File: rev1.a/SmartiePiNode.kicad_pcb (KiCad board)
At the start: 2 copper layers, 71.7 x 55 mm, 53 parts, among them CN1 USBMICROb, CN2 ST-LINK, CN3 SX1238_TRX_HEADER, SW1 SW_PUSH, U1 ISL91127IR, U2 STM32L052_LQFP48, X1 abm10, X2 ABS25-32.768KHZ-6-T

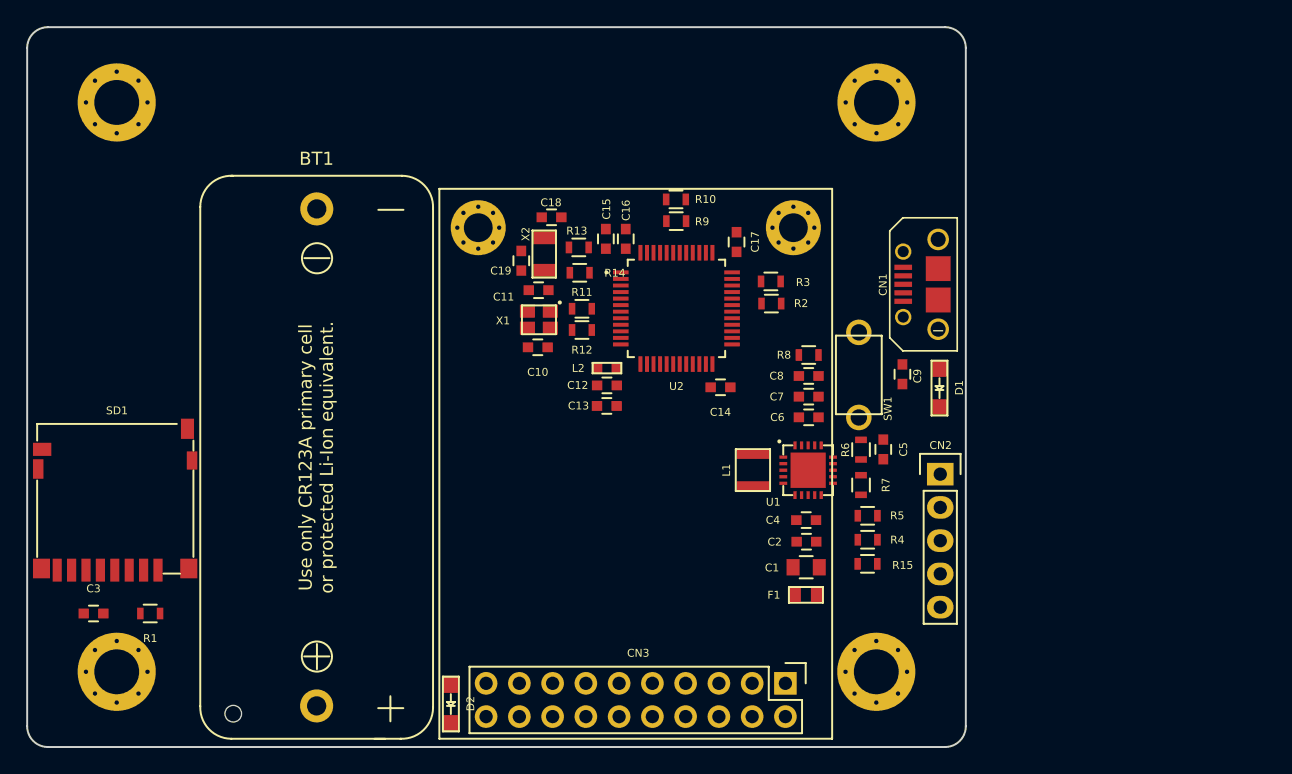
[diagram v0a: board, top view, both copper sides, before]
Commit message: footprint placement and tweaking continued...
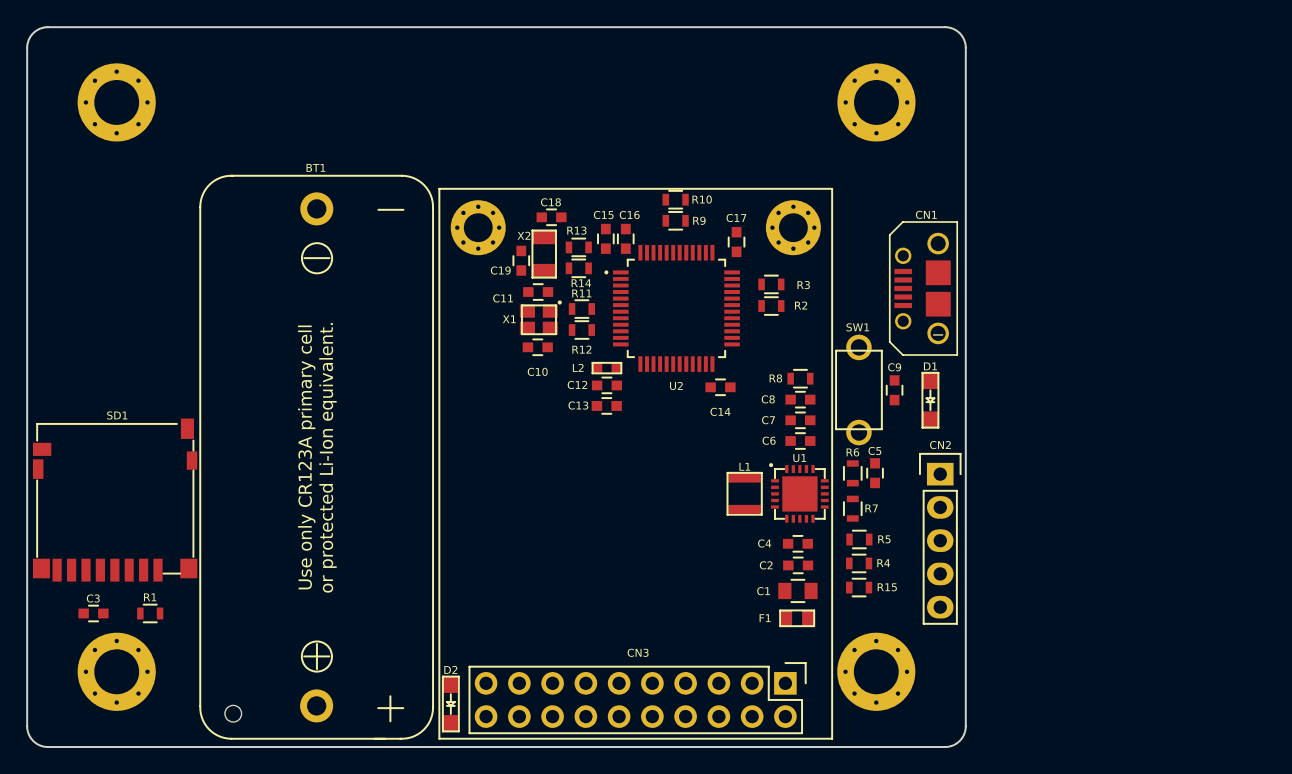
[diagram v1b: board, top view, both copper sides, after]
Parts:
- moved R4 1.92 mm to (162.6, 136.6), turned to 180 degrees
- moved R15 1.92 mm to (162.6, 138.5)
- moved U1 1.92 mm to (158.1, 131.3)
- moved C1 1.92 mm to (157.9, 138.7)
- moved C2 1.92 mm to (157.9, 136.8)
- moved C4 1.92 mm to (157.9, 135.1)
- moved C5 1.92 mm to (163.8, 129.7)
- moved C6 1.92 mm to (158.1, 127.3)
- moved C7 1.92 mm to (158.1, 125.7)
- moved L1 1.92 mm to (153.9, 131.3)
- moved R5 1.92 mm to (162.6, 134.8)
- moved R7 1.92 mm to (162.1, 132.5)
- moved R8 1.92 mm to (158.1, 122.5)
- moved C8 1.92 mm to (158.1, 124.1)
- moved R6 1.92 mm to (162.1, 129.8)
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
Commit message: usb and schematic changes/tweaks.
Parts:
- added CN4: VIN, Pin_Headers:Pin_Header_Straight_1x02, F.Cu at (168.8, 143.6)
- added R16: 100K, Resistors_SMD:R_0603, F.Cu at (163.6, 112.1)
- added R17: 1.5K, Resistors_SMD:R_0603, F.Cu at (163.6, 114.7)
- CN2: value ST-LINK -> SWD
- moved CN1 0.20 mm to (167.2, 115.8)

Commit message: added battery sensing circuit and a bit more work on usb.
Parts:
- added C20: DNP, Capacitors_SMD:C_0603, F.Cu at (181.1, 119.0)
- added R18: DNP, Resistors_SMD:R_0603, F.Cu at (181.1, 124.9)
- added R19: DNP, Resistors_SMD:R_0603, F.Cu at (184.7, 119.0)
- added R20: DNP, Resistors_SMD:R_0603, F.Cu at (188.3, 119.0)
- added R21: DNP, Resistors_SMD:R_0603, F.Cu at (191.9, 119.0)
- added R22: DNP, Resistors_SMD:R_0603, F.Cu at (184.7, 124.9)
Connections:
- R17 pad 1: /+3V3 -> /USB_RENUMn
- U2 pad 11: /+VBAT -> Net-(U2-Pad11)
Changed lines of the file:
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@@
 (kicad_pcb (version 20160815) (host pcbnew "(2017-01-24 revision 0b6147e)-makepkg")
   (general
-    (links 182)
-    (no_connects 134)
+    (links 189)
+    (no_connects 141)
     (area 98.984999 95.604999 170.825001 150.735001)
     (thickness 1.6)
@@
     (tracks 1)
     (zones 0)
-    (modules 56)
-    (nets 74)
+    (modules 62)
+    (nets 79)
   )
   (page A4)
@@
   (net 72 "Net-(R15-Pad1)")
   (net 73 "Net-(CN4-Pad1)")
+  (net 74 /VMEASURE)
+  (net 75 /USB_RENUMn)
+  (net 76 "Net-(R19-Pad2)")
+  (net 77 /VSENSE)
+  (net 78 "Net-(U2-Pad11)")
   (net_class Default "This is the default net class."
     (clearance 0.2)
@@
     (add_net /USB_DM)
     (add_net /USB_DP)
+    (add_net /USB_RENUMn)
+    (add_net /VMEASURE)
+    (add_net /VSENSE)
     (add_net GND)
     (add_net "Net-(C10-Pad2)")
@@
     (add_net "Net-(R14-Pad2)")
     (add_net "Net-(R15-Pad1)")
+    (add_net "Net-(R19-Pad2)")
     (add_net "Net-(R4-Pad1)")
     (add_net "Net-(SD1-Pad1)")
@@
     (add_net "Net-(U1-Pad16)")
     (add_net "Net-(U2-Pad10)")
+    (add_net "Net-(U2-Pad11)")
     (add_net "Net-(U2-Pad12)")
     (add_net "Net-(U2-Pad13)")
@@
       (net 69 "Net-(U2-Pad12)"))
     (pad 11 smd rect (at -4.249999 2.250001) (size 1.1938 0.3048) (layers F.Cu F.Paste F.Mask)
-      (net 2 /+VBAT))
+      (net 78 "Net-(U2-Pad11)"))
     (pad 10 smd rect (at -4.249999 1.749999) (size 1.1938 0.3048) (layers F.Cu F.Paste F.Mask)
       (net 70 "Net-(U2-Pad10)"))
@@
     (fp_line (start -0.5 -0.675) (end 0.5 -0.675) (layer F.SilkS) (width 0.15))
     (pad 1 smd rect (at -0.75 0 270) (size 0.5 0.9) (layers F.Cu F.Paste F.Mask)
-      (net 4 /+3V3))
+      (net 75 /USB_RENUMn))
     (pad 2 smd rect (at 0.75 0 270) (size 0.5 0.9) (layers F.Cu F.Paste F.Mask)
       (net 14 "Net-(CN1-Pad3)"))
@@
     )
   )
+  (module Capacitors_SMD:C_0603 (layer F.Cu)
+    (at 181.119408 119.033318)
+    (descr "Capacitor SMD 0603, reflow soldering, AVX (see smccp.pdf)")
+    (tags "capacitor 0603")
+    (attr smd)
+    (fp_text reference C20 (at 0 -1.9) (layer F.SilkS)
+      (effects (font (size 1 1) (thickness 0.15)))
+    )
+    (fp_text value DNP (at 0 1.9) (layer F.Fab)
+      (effects (font (size 1 1) (thickness 0.15)))
+    )
+    (fp_line (start -1.45 -0.75) (end 1.45 -0.75) (layer F.CrtYd) (width 0.05))
+    (fp_line (start -1.45 0.75) (end 1.45 0.75) (layer F.CrtYd) (width 0.05))
+    (fp_line (start -1.45 -0.75) (end -1.45 0.75) (layer F.CrtYd) (width 0.05))
+    (fp_line (start 1.45 -0.75) (end 1.45 0.75) (layer F.CrtYd) (width 0.05))
+    (fp_line (start -0.35 -0.6) (end 0.35 -0.6) (layer F.SilkS) (width 0.15))
+    (fp_line (start 0.35 0.6) (end -0.35 0.6) (layer F.SilkS) (width 0.15))
+    (pad 1 smd rect (at -0.75 0) (size 0.8 0.75) (layers F.Cu F.Paste F.Mask)
+      (net 74 /VMEASURE))
+    (pad 2 smd rect (at 0.75 0) (size 0.8 0.75) (layers F.Cu F.Paste F.Mask)
+      (net 1 GND))
+    (model Capacitors_SMD.3dshapes/C_0603.wrl
+      (at (xyz 0 0 0))
+      (scale (xyz 1 1 1))
+      (rotate (xyz 0 0 0))
+    )
+  )
+  (module Resistors_SMD:R_0603 (layer F.Cu)
+    (at 181.119408 124.883318)
+    (descr "Resistor SMD 0603, reflow soldering, Vishay (see dcrcw.pdf)")
+    (tags "resistor 0603")
+    (attr smd)
+    (fp_text reference R18 (at 0 -1.9) (layer F.SilkS)
+      (effects (font (size 1 1) (thickness 0.15)))
+    )
+    (fp_text value DNP (at 0 1.9) (layer F.Fab)
+      (effects (font (size 1 1) (thickness 0.15)))
+    )
+    (fp_line (start -0.5 -0.675) (end 0.5 -0.675) (layer F.SilkS) (width 0.15))
+    (fp_line (start 0.5 0.675) (end -0.5 0.675) (layer F.SilkS) (width 0.15))
+    (fp_line (start 1.3 -0.8) (end 1.3 0.8) (layer F.CrtYd) (width 0.05))
+    (fp_line (start -1.3 -0.8) (end -1.3 0.8) (layer F.CrtYd) (width 0.05))
+    (fp_line (start -1.3 0.8) (end 1.3 0.8) (layer F.CrtYd) (width 0.05))
+    (fp_line (start -1.3 -0.8) (end 1.3 -0.8) (layer F.CrtYd) (width 0.05))
+    (pad 2 smd rect (at 0.75 0) (size 0.5 0.9) (layers F.Cu F.Paste F.Mask)
+      (net 14 "Net-(CN1-Pad3)"))
+    (pad 1 smd rect (at -0.75 0) (size 0.5 0.9) (layers F.Cu F.Paste F.Mask)
+      (net 4 /+3V3))
+    (model Resistors_SMD.3dshapes/R_0603.wrl
+      (at (xyz 0 0 0))
+      (scale (xyz 1 1 1))
+      (rotate (xyz 0 0 0))
+    )
+  )
+  (module Resistors_SMD:R_0603 (layer F.Cu)
+    (at 184.709408 119.033318)
+    (descr "Resistor SMD 0603, reflow soldering, Vishay (see dcrcw.pdf)")
+    (tags "resistor 0603")
+    (attr smd)
+    (fp_text reference R19 (at 0 -1.9) (layer F.SilkS)
+      (effects (font (size 1 1) (thickness 0.15)))
+    )
+    (fp_text value DNP (at 0 1.9) (layer F.Fab)
+      (effects (font (size 1 1) (thickness 0.15)))
+    )
+    (fp_line (start -1.3 -0.8) (end 1.3 -0.8) (layer F.CrtYd) (width 0.05))
+    (fp_line (start -1.3 0.8) (end 1.3 0.8) (layer F.CrtYd) (width 0.05))
+    (fp_line (start -1.3 -0.8) (end -1.3 0.8) (layer F.CrtYd) (width 0.05))
+    (fp_line (start 1.3 -0.8) (end 1.3 0.8) (layer F.CrtYd) (width 0.05))
+    (fp_line (start 0.5 0.675) (end -0.5 0.675) (layer F.SilkS) (width 0.15))
+    (fp_line (start -0.5 -0.675) (end 0.5 -0.675) (layer F.SilkS) (width 0.15))
+    (pad 1 smd rect (at -0.75 0) (size 0.5 0.9) (layers F.Cu F.Paste F.Mask)
+      (net 2 /+VBAT))
+    (pad 2 smd rect (at 0.75 0) (size 0.5 0.9) (layers F.Cu F.Paste F.Mask)
+      (net 76 "Net-(R19-Pad2)"))
+    (model Resistors_SMD.3dshapes/R_0603.wrl
+      (at (xyz 0 0 0))
+      (scale (xyz 1 1 1))
+      (rotate (xyz 0 0 0))
+    )
+  )
+  (module Resistors_SMD:R_0603 (layer F.Cu)
+    (at 188.299408 119.033318)
+    (descr "Resistor SMD 0603, reflow soldering, Vishay (see dcrcw.pdf)")
+    (tags "resistor 0603")
+    (attr smd)
+    (fp_text reference R20 (at 0 -1.9) (layer F.SilkS)
+      (effects (font (size 1 1) (thickness 0.15)))
+    )
+    (fp_text value DNP (at 0 1.9) (layer F.Fab)
+      (effects (font (size 1 1) (thickness 0.15)))
+    )
+    (fp_line (start -0.5 -0.675) (end 0.5 -0.675) (layer F.SilkS) (width 0.15))
+    (fp_line (start 0.5 0.675) (end -0.5 0.675) (layer F.SilkS) (width 0.15))
+    (fp_line (start 1.3 -0.8) (end 1.3 0.8) (layer F.CrtYd) (width 0.05))
+    (fp_line (start -1.3 -0.8) (end -1.3 0.8) (layer F.CrtYd) (width 0.05))
+    (fp_line (start -1.3 0.8) (end 1.3 0.8) (layer F.CrtYd) (width 0.05))
+    (fp_line (start -1.3 -0.8) (end 1.3 -0.8) (layer F.CrtYd) (width 0.05))
+    (pad 2 smd rect (at 0.75 0) (size 0.5 0.9) (layers F.Cu F.Paste F.Mask)
+      (net 1 GND))
+    (pad 1 smd rect (at -0.75 0) (size 0.5 0.9) (layers F.Cu F.Paste F.Mask)
+      (net 76 "Net-(R19-Pad2)"))
+    (model Resistors_SMD.3dshapes/R_0603.wrl
+      (at (xyz 0 0 0))
+      (scale (xyz 1 1 1))
+      (rotate (xyz 0 0 0))
+    )
+  )
+  (module Resistors_SMD:R_0603 (layer F.Cu)
+    (at 191.889408 119.033318)
+    (descr "Resistor SMD 0603, reflow soldering, Vishay (see dcrcw.pdf)")
+    (tags "resistor 0603")
+    (attr smd)
+    (fp_text reference R21 (at 0 -1.9) (layer F.SilkS)
+      (effects (font (size 1 1) (thickness 0.15)))
+    )
+    (fp_text value DNP (at 0 1.9) (layer F.Fab)
+      (effects (font (size 1 1) (thickness 0.15)))
+    )
+    (fp_line (start -0.5 -0.675) (end 0.5 -0.675) (layer F.SilkS) (width 0.15))
+    (fp_line (start 0.5 0.675) (end -0.5 0.675) (layer F.SilkS) (width 0.15))
+    (fp_line (start 1.3 -0.8) (end 1.3 0.8) (layer F.CrtYd) (width 0.05))
+    (fp_line (start -1.3 -0.8) (end -1.3 0.8) (layer F.CrtYd) (width 0.05))
+    (fp_line (start -1.3 0.8) (end 1.3 0.8) (layer F.CrtYd) (width 0.05))
+    (fp_line (start -1.3 -0.8) (end 1.3 -0.8) (layer F.CrtYd) (width 0.05))
+    (pad 2 smd rect (at 0.75 0) (size 0.5 0.9) (layers F.Cu F.Paste F.Mask)
+      (net 77 /VSENSE))
+    (pad 1 smd rect (at -0.75 0) (size 0.5 0.9) (layers F.Cu F.Paste F.Mask)
+      (net 76 "Net-(R19-Pad2)"))
+    (model Resistors_SMD.3dshapes/R_0603.wrl
+      (at (xyz 0 0 0))
+      (scale (xyz 1 1 1))
+      (rotate (xyz 0 0 0))
+    )
+  )
+  (module Resistors_SMD:R_0603 (layer F.Cu)
+    (at 184.709408 124.883318)
+    (descr "Resistor SMD 0603, reflow soldering, Vishay (see dcrcw.pdf)")
+    (tags "resistor 0603")
+    (attr smd)
+    (fp_text reference R22 (at 0 -1.9) (layer F.SilkS)
+      (effects (font (size 1 1) (thickness 0.15)))
+    )
+    (fp_text value DNP (at 0 1.9) (layer F.Fab)
+      (effects (font (size 1 1) (thickness 0.15)))
+    )
+    (fp_line (start -1.3 -0.8) (end 1.3 -0.8) (layer F.CrtYd) (width 0.05))
+    (fp_line (start -1.3 0.8) (end 1.3 0.8) (layer F.CrtYd) (width 0.05))
+    (fp_line (start -1.3 -0.8) (end -1.3 0.8) (layer F.CrtYd) (width 0.05))
+    (fp_line (start 1.3 -0.8) (end 1.3 0.8) (layer F.CrtYd) (width 0.05))
+    (fp_line (start 0.5 0.675) (end -0.5 0.675) (layer F.SilkS) (width 0.15))
+    (fp_line (start -0.5 -0.675) (end 0.5 -0.675) (layer F.SilkS) (width 0.15))
+    (pad 1 smd rect (at -0.75 0) (size 0.5 0.9) (layers F.Cu F.Paste F.Mask)
+      (net 74 /VMEASURE))
+    (pad 2 smd rect (at 0.75 0) (size 0.5 0.9) (layers F.Cu F.Paste F.Mask)
+      (net 76 "Net-(R19-Pad2)"))
+    (model Resistors_SMD.3dshapes/R_0603.wrl
+      (at (xyz 0 0 0))
+      (scale (xyz 1 1 1))
+      (rotate (xyz 0 0 0))
+    )
+  )

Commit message: battery sense circuit and new footprint for voltage reg.
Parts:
- moved R21 58.4 mm to (133.6, 120.4), turned to 180 degrees
- moved R20 54.8 mm to (133.6, 122.5), turned to 180 degrees
- moved R19 51.1 mm to (133.9, 124.6)
- moved R22 46.8 mm to (138.0, 122.8)
- moved C20 43.5 mm to (138.0, 124.4)
- moved R18 21.7 mm to (161.9, 114.7), turned to 270 degrees
- moved U1 0.08 mm to (158.1, 131.3)

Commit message: more pcb layout
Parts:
- moved R20 2.11 mm to (133.9, 120.4)
- moved R21 2.02 mm to (133.8, 122.4), turned to 0 degrees
- turned R22 to 180 degrees
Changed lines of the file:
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@@
     (tags "capacitor 0603")
     (attr smd)
-    (fp_text reference C10 (at 0.03 -1.17 180) (layer F.SilkS)
+    (fp_text reference C10 (at 2.16 0 180) (layer F.SilkS)
       (effects (font (size 0.6 0.6) (thickness 0.1)))
     )
@@
     (tags "capacitor 0603")
     (attr smd)
-    (fp_text reference C20 (at 0 1.19) (layer F.SilkS)
+    (fp_text reference C20 (at -2.06 0.01) (layer F.SilkS)
       (effects (font (size 0.6 0.6) (thickness 0.1)))
     )
@@
   )
   (module Resistors_SMD:R_0603 (layer F.Cu)
-    (at 133.6 122.45 180)
+    (at 133.86 120.36 180)
     (descr "Resistor SMD 0603, reflow soldering, Vishay (see dcrcw.pdf)")
     (tags "resistor 0603")
@@
   )
   (module Resistors_SMD:R_0603 (layer F.Cu)
-    (at 133.55 120.44 180)
-    (descr "Resistor SMD 0603, reflow soldering, Vishay (see dcrcw.pdf)")
-    (tags "resistor 0603")
-    (attr smd)
-    (fp_text reference R21 (at 1.98 -0.01 180) (layer F.SilkS)
+    (at 133.84 122.44)
+    (descr "Resistor SMD 0603, reflow soldering, Vishay (see dcrcw.pdf)")
+    (tags "resistor 0603")
+    (attr smd)
+    (fp_text reference R21 (at -2.01 0) (layer F.SilkS)
+      (effects (font (size 0.6 0.6) (thickness 0.1)))
+    )
+    (fp_text value DNP (at 0 1.9) (layer F.Fab)
+      (effects (font (size 0.6 0.6) (thickness 0.1)))
+    )
+    (fp_line (start -0.5 -0.675) (end 0.5 -0.675) (layer F.SilkS) (width 0.15))
+    (fp_line (start 0.5 0.675) (end -0.5 0.675) (layer F.SilkS) (width 0.15))
+    (fp_line (start 1.3 -0.8) (end 1.3 0.8) (layer F.CrtYd) (width 0.05))
+    (fp_line (start -1.3 -0.8) (end -1.3 0.8) (layer F.CrtYd) (width 0.05))
+    (fp_line (start -1.3 0.8) (end 1.3 0.8) (layer F.CrtYd) (width 0.05))
+    (fp_line (start -1.3 -0.8) (end 1.3 -0.8) (layer F.CrtYd) (width 0.05))
+    (pad 2 smd rect (at 0.75 0) (size 0.5 0.9) (layers F.Cu F.Paste F.Mask)
+      (net 77 /VSENSE))
+    (pad 1 smd rect (at -0.75 0) (size 0.5 0.9) (layers F.Cu F.Paste F.Mask)
+      (net 76 "Net-(R19-Pad2)"))
+    (model Resistors_SMD.3dshapes/R_0603.wrl
+      (at (xyz 0 0 0))
+      (scale (xyz 1 1 1))
+      (rotate (xyz 0 0 0))
+    )
+  )
+  (module Resistors_SMD:R_0603 (layer F.Cu)
+    (at 137.96 122.75 180)
+    (descr "Resistor SMD 0603, reflow soldering, Vishay (see dcrcw.pdf)")
+    (tags "resistor 0603")
+    (attr smd)
+    (fp_text reference R22 (at 2.09 0 180) (layer F.SilkS)
       (effects (font (size 0.6 0.6) (thickness 0.1)))
     )
@@
       (effects (font (size 0.6 0.6) (thickness 0.1)))
     )
-    (fp_line (start -0.5 -0.675) (end 0.5 -0.675) (layer F.SilkS) (width 0.15))
-    (fp_line (start 0.5 0.675) (end -0.5 0.675) (layer F.SilkS) (width 0.15))
-    (fp_line (start 1.3 -0.8) (end 1.3 0.8) (layer F.CrtYd) (width 0.05))
-    (fp_line (start -1.3 -0.8) (end -1.3 0.8) (layer F.CrtYd) (width 0.05))
-    (fp_line (start -1.3 0.8) (end 1.3 0.8) (layer F.CrtYd) (width 0.05))
-    (fp_line (start -1.3 -0.8) (end 1.3 -0.8) (layer F.CrtYd) (width 0.05))
+    (fp_line (start -1.3 -0.8) (end 1.3 -0.8) (layer F.CrtYd) (width 0.05))
+    (fp_line (start -1.3 0.8) (end 1.3 0.8) (layer F.CrtYd) (width 0.05))
+    (fp_line (start -1.3 -0.8) (end -1.3 0.8) (layer F.CrtYd) (width 0.05))
+    (fp_line (start 1.3 -0.8) (end 1.3 0.8) (layer F.CrtYd) (width 0.05))
+    (fp_line (start 0.5 0.675) (end -0.5 0.675) (layer F.SilkS) (width 0.15))
+    (fp_line (start -0.5 -0.675) (end 0.5 -0.675) (layer F.SilkS) (width 0.15))
+    (pad 1 smd rect (at -0.75 0 180) (size 0.5 0.9) (layers F.Cu F.Paste F.Mask)
+      (net 74 /VMEASURE))
     (pad 2 smd rect (at 0.75 0 180) (size 0.5 0.9) (layers F.Cu F.Paste F.Mask)
-      (net 77 /VSENSE))
-    (pad 1 smd rect (at -0.75 0 180) (size 0.5 0.9) (layers F.Cu F.Paste F.Mask)
-      (net 76 "Net-(R19-Pad2)"))
-    (model Resistors_SMD.3dshapes/R_0603.wrl
-      (at (xyz 0 0 0))
-      (scale (xyz 1 1 1))
-      (rotate (xyz 0 0 0))
-    )
-  )
-  (module Resistors_SMD:R_0603 (layer F.Cu)
-    (at 137.97 122.75)
-    (descr "Resistor SMD 0603, reflow soldering, Vishay (see dcrcw.pdf)")
-    (tags "resistor 0603")
-    (attr smd)
-    (fp_text reference R22 (at -2.22 -0.01) (layer F.SilkS)
-      (effects (font (size 0.6 0.6) (thickness 0.1)))
-    )
-    (fp_text value DNP (at 0 1.9) (layer F.Fab)
-      (effects (font (size 0.6 0.6) (thickness 0.1)))
-    )
-    (fp_line (start -1.3 -0.8) (end 1.3 -0.8) (layer F.CrtYd) (width 0.05))
-    (fp_line (start -1.3 0.8) (end 1.3 0.8) (layer F.CrtYd) (width 0.05))
-    (fp_line (start -1.3 -0.8) (end -1.3 0.8) (layer F.CrtYd) (width 0.05))
-    (fp_line (start 1.3 -0.8) (end 1.3 0.8) (layer F.CrtYd) (width 0.05))
-    (fp_line (start 0.5 0.675) (end -0.5 0.675) (layer F.SilkS) (width 0.15))
-    (fp_line (start -0.5 -0.675) (end 0.5 -0.675) (layer F.SilkS) (width 0.15))
-    (pad 1 smd rect (at -0.75 0) (size 0.5 0.9) (layers F.Cu F.Paste F.Mask)
-      (net 74 /VMEASURE))
-    (pad 2 smd rect (at 0.75 0) (size 0.5 0.9) (layers F.Cu F.Paste F.Mask)
       (net 76 "Net-(R19-Pad2)"))
     (model Resistors_SMD.3dshapes/R_0603.wrl
@@
   (module intersil-isl91127ir:intersil-isl91127ir (layer F.Cu)
     (at 158.11 131.26)
-    (fp_text reference U1 (at 3.76 10.41) (layer F.SilkS)
-      (effects (font (size 1 1) (thickness 0.15)))
+    (fp_text reference U1 (at -0.04 -2.72) (layer F.SilkS)
+      (effects (font (size 0.6 0.6) (thickness 0.1)))
     )
     (fp_text value ISL91127IR (at 3.75 -9.88) (layer F.Fab)
-      (effects (font (size 1 1) (thickness 0.15)))
+      (effects (font (size 0.6 0.6) (thickness 0.1)))
     )
     (fp_circle (center -2.2 -2.2) (end -2.15 -2.14) (layer F.SilkS) (width 0.15))

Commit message: finalizing layout
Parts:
- moved R20 0.64 mm to (133.9, 121.0)
- moved C5 0.56 mm to (163.8, 130.3)
- moved R6 0.54 mm to (162.1, 130.3)
- moved R7 0.54 mm to (162.1, 133.0)
- moved C6 0.51 mm to (158.1, 127.8)
- moved C7 0.49 mm to (158.1, 126.2)
- moved C8 0.47 mm to (158.1, 124.6)
- moved R8 0.47 mm to (158.1, 123.0)
- moved R5 0.39 mm to (162.6, 135.2)
- moved L1 0.32 mm to (153.6, 131.5)
- moved R21 0.27 mm to (133.9, 122.7)
- moved R17 0.26 mm to (163.6, 115.0)
- moved R18 0.26 mm to (161.9, 115.0)
- moved R16 0.24 mm to (163.6, 112.3)
- moved U1 0.24 mm to (158.1, 131.5)
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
